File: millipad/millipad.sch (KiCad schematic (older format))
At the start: 51 parts, among them SW1 SW_Push, SW2 Rotary_Encoder_Switch, U1 ATmega32U4-AU, U2 PRTR5V0U2X, Y1 16MHz

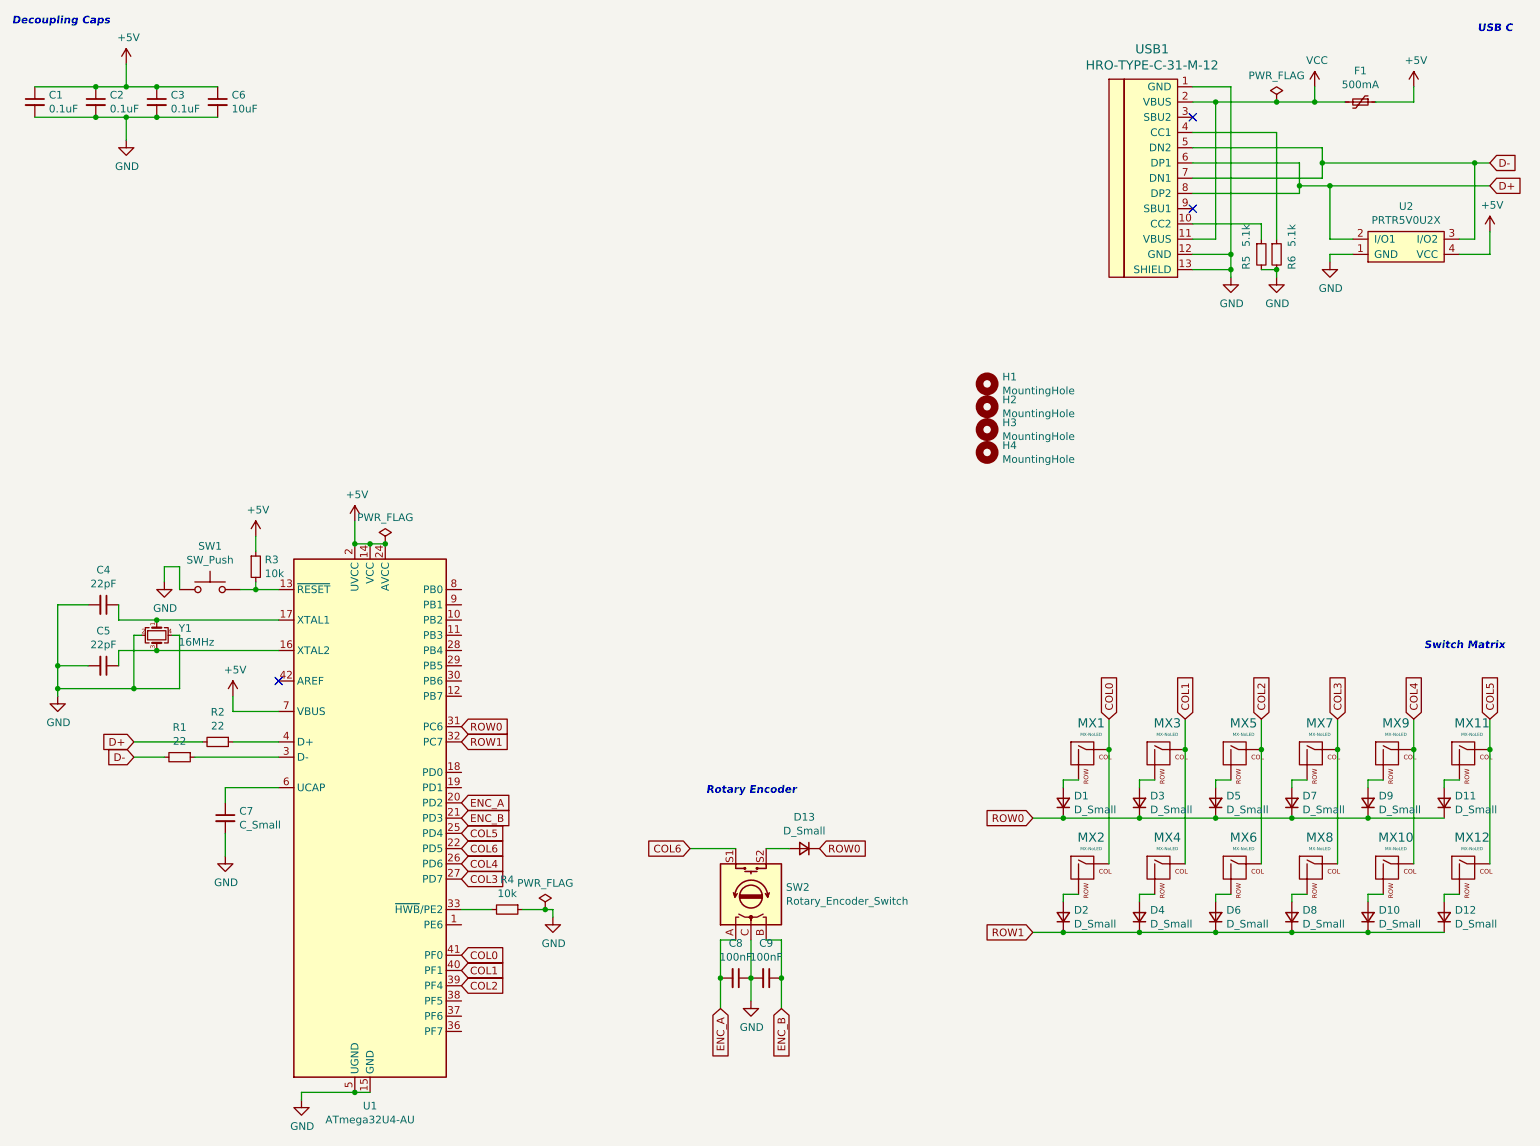
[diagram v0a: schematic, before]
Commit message: OLED Implementation WIP
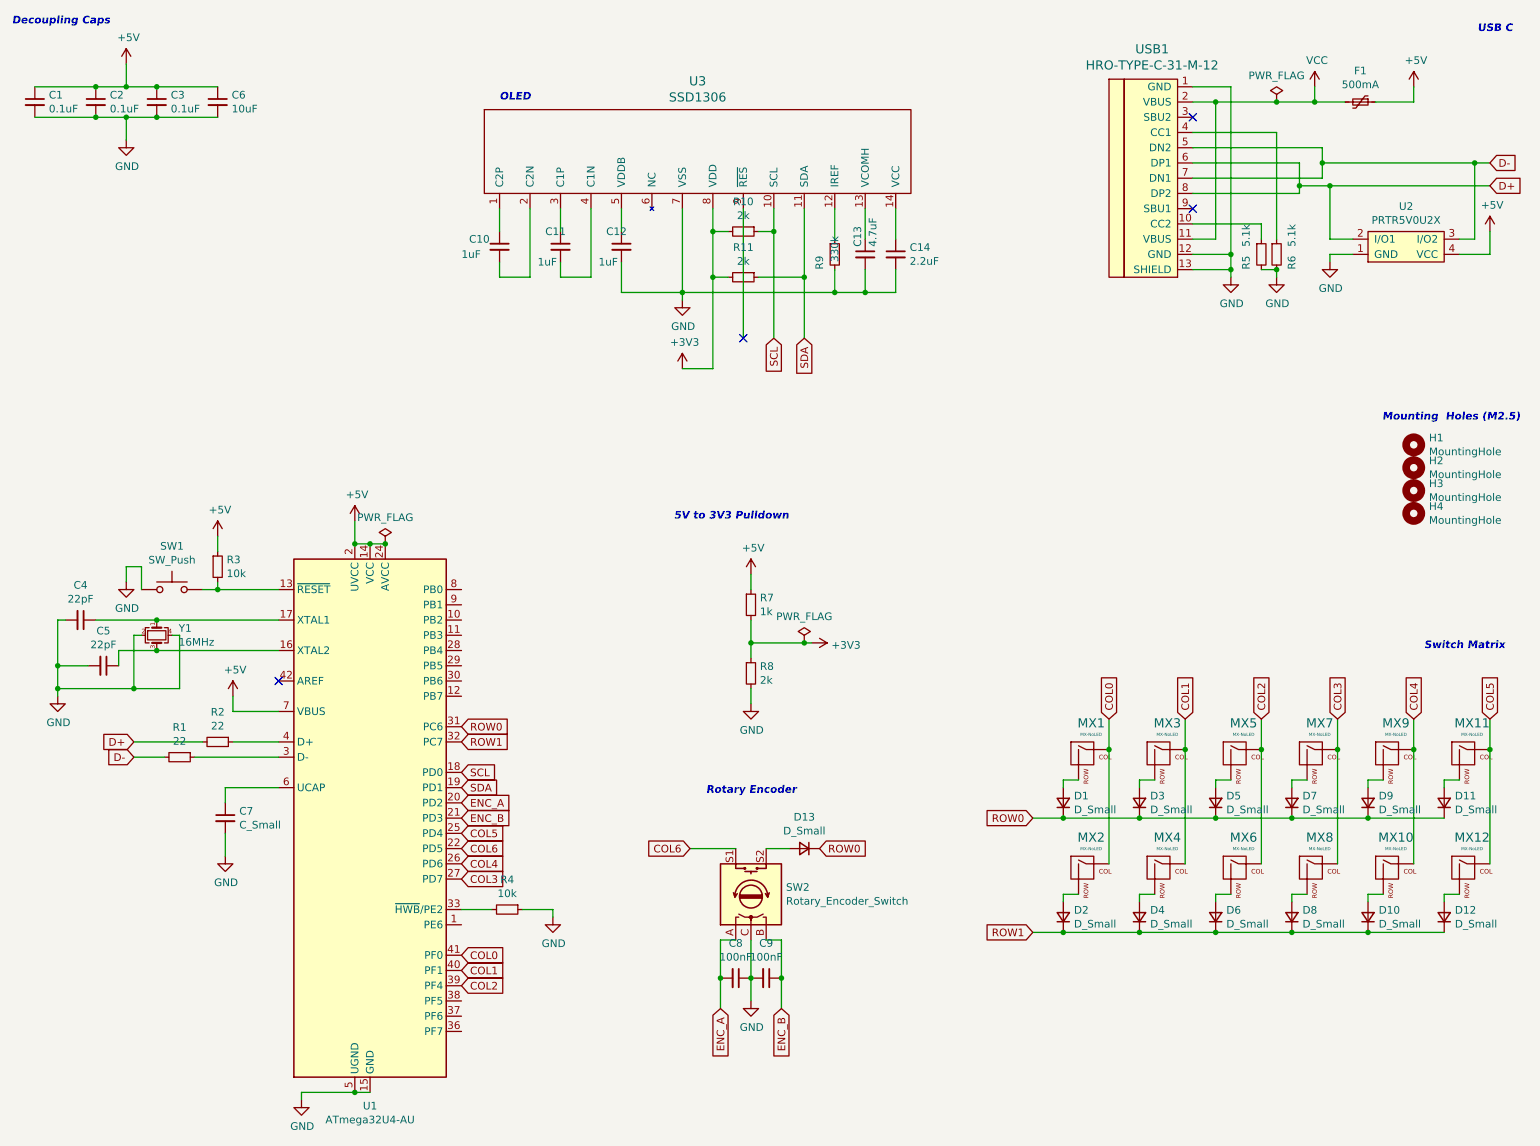
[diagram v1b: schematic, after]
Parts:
- added C10, C11, C12: 1uF, Capacitor_SMD:C_0805_2012Metric, symbol Device:C_Small
- added C13: 4.7uF, Capacitor_SMD:C_0805_2012Metric, symbol Device:C_Small
- added C14: 2.2uF, Capacitor_SMD:C_0805_2012Metric, symbol Device:C_Small
- added R10, R11, R8: 2k, Resistor_SMD:R_0805_2012Metric, symbol Device:R_Small
- added R7: 1k, Resistor_SMD:R_0805_2012Metric, symbol Device:R_Small
- added R9: 330k, Resistor_SMD:R_0805_2012Metric, symbol Device:R_Small
- added U3: SSD1306, KiCad-SSD1306_OLED-0.91-128x32:SSD1306_OLED-0.91-128x32, symbol SSD1306_OLED-0.91-128x32:SSD1306
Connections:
- net +5V: now also R7.1
- net GND: now also C12.2, C13.2, C14.2, R8.2, R9.2, U3.7 (VSS)
- net SCL: now reaches U1.18 (PD0)
- net SCL: now also R10.1, U3.10 (SCL)
- net SDA: now reaches U1.19 (PD1)
- net SDA: now also R11.1, U3.11 (SDA)
- new net: C10.1, U3.1 (C2P)
- new net: R9.1, U3.12 (IREF)
- new net: C13.1, U3.13 (VCOMH)
- new net: C14.1, U3.14 (VCC)
- new net: C10.2, U3.2 (C2N)
- new net: C11.1, U3.3 (C1P)
- new net: C11.2, U3.4 (C1N)
- new net: C12.1, U3.5 (VDDB)
- new net +3V3: R10.2, R11.2, R7.2, R8.1, U3.8 (VDD)
- no-connect marks 3 -> 4
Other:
- note added: "5V to 3V3 Pulldown"
- note added: "Mounting Holes (M2.5)"
- note added: "OLED"
- moved on the sheet: C4, H1, H2, H3, H4, R3, SW1
